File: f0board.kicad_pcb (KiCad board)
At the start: 2 copper layers, 31 x 18.3 mm, 28 parts, among them P1 CONN_12, P2 CONN_12, SW1 SW_PUSH, U1 STM32F303CCT6, U2 MCP1700, U3 MAX3051, X1 XTAL-SMD-4-PADS

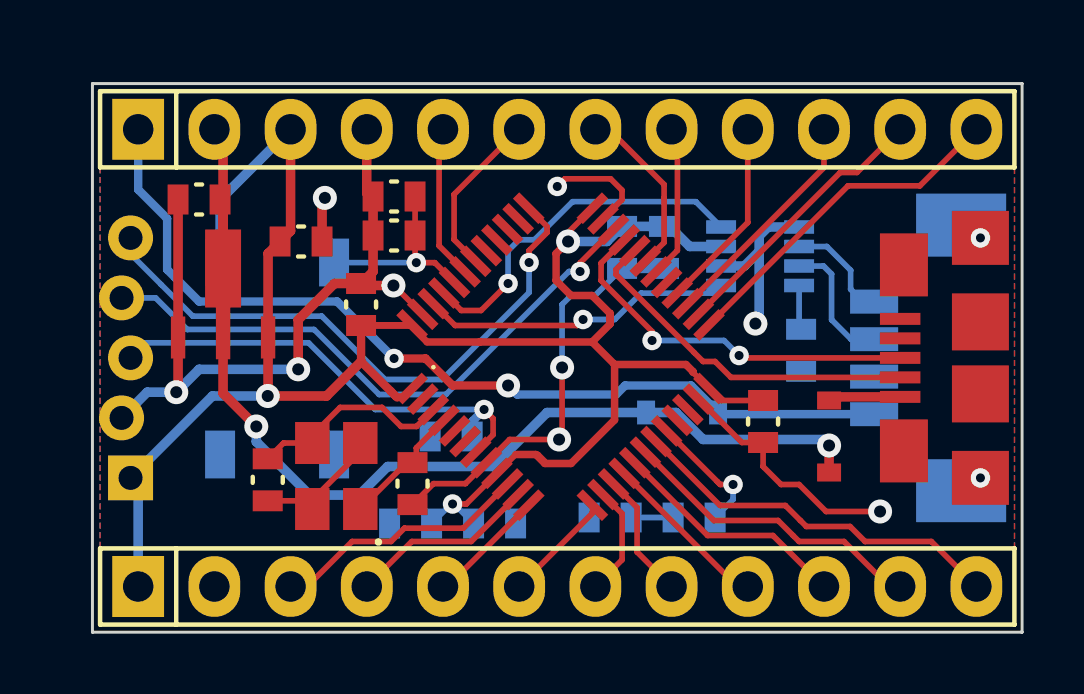
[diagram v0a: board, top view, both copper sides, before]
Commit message: inch grid alignment.
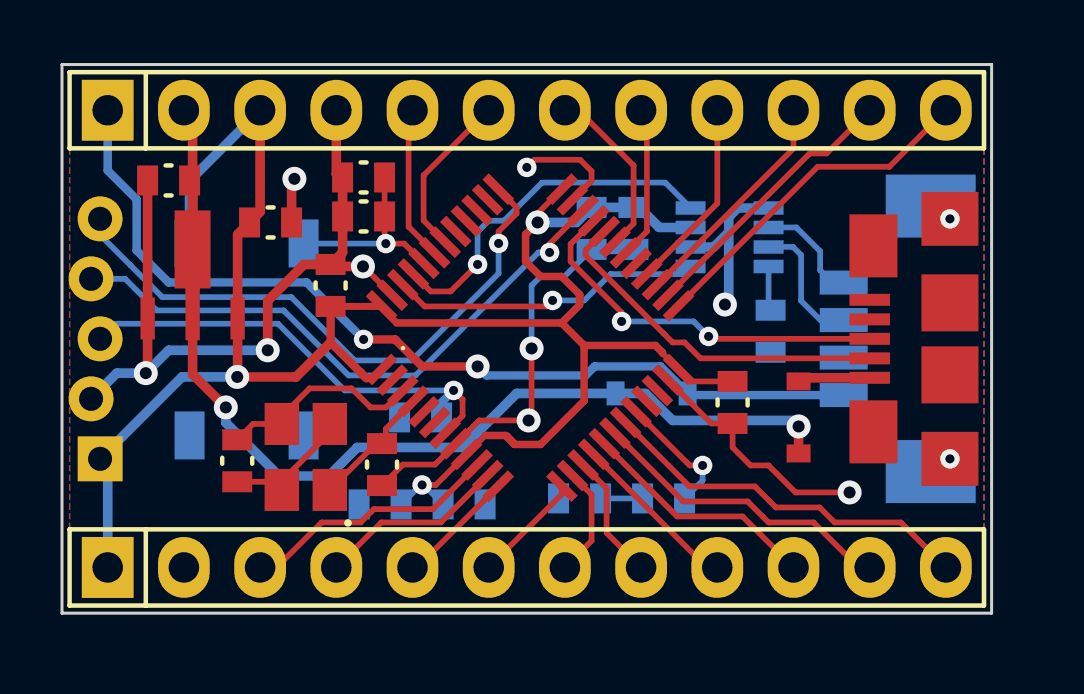
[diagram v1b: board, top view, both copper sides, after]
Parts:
- moved R3 1.20 mm to (50.0, 32.8)
- moved C7 1.20 mm to (35.4, 31.2)
- moved P1 1.20 mm to (41.9, 25.4)
- moved C12 1.20 mm to (33.4, 29.1)
- moved C4 1.20 mm to (38.4, 35.6)
- moved P2 1.20 mm to (41.9, 40.6)
- moved X1 1.20 mm to (34.5, 37.0)
- moved C11 1.20 mm to (30.0, 27.7)
- moved CONN1 1.20 mm to (27.7, 33.0)
- moved U2 1.20 mm to (30.8, 31.6)
- moved C2 1.20 mm to (45.5, 29.3)
- moved C3 1.20 mm to (44.1, 29.3)
- moved U3 1.20 mm to (47.4, 30.6)
- moved C1 1.20 mm to (36.5, 28.9)
- moved C10 1.20 mm to (32.3, 37.1)
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
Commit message: Move LED for silkscreen.
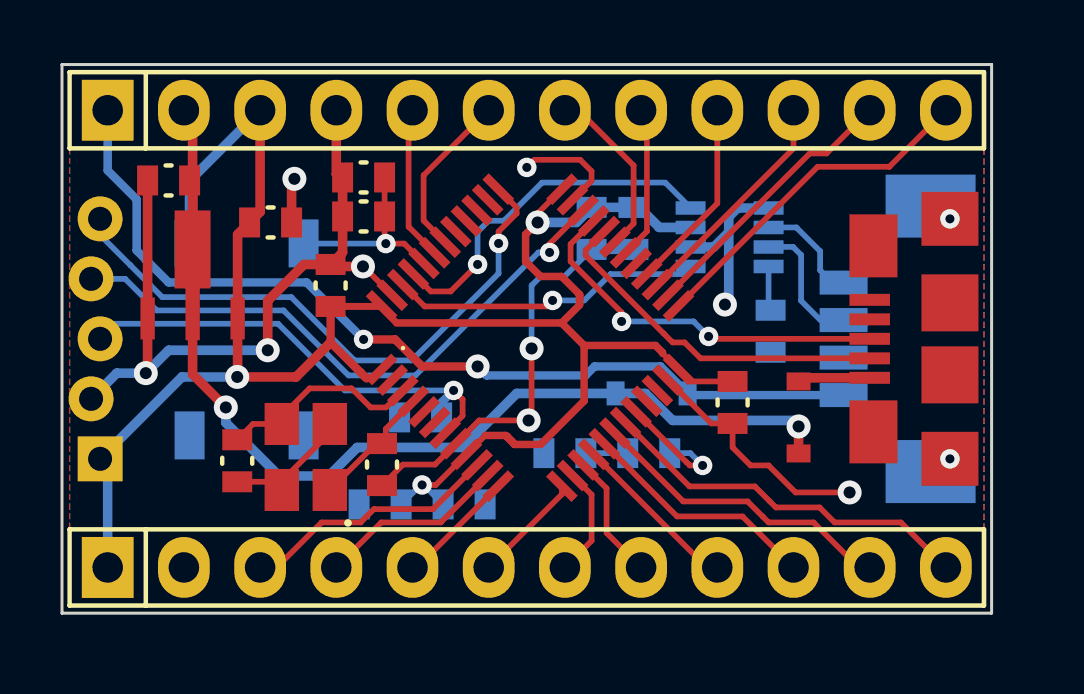
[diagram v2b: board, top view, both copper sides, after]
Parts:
- moved D1 1.59 mm to (46.0, 36.8)
- moved R1 1.59 mm to (43.2, 36.8)

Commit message: Move more compontents for silkscreen
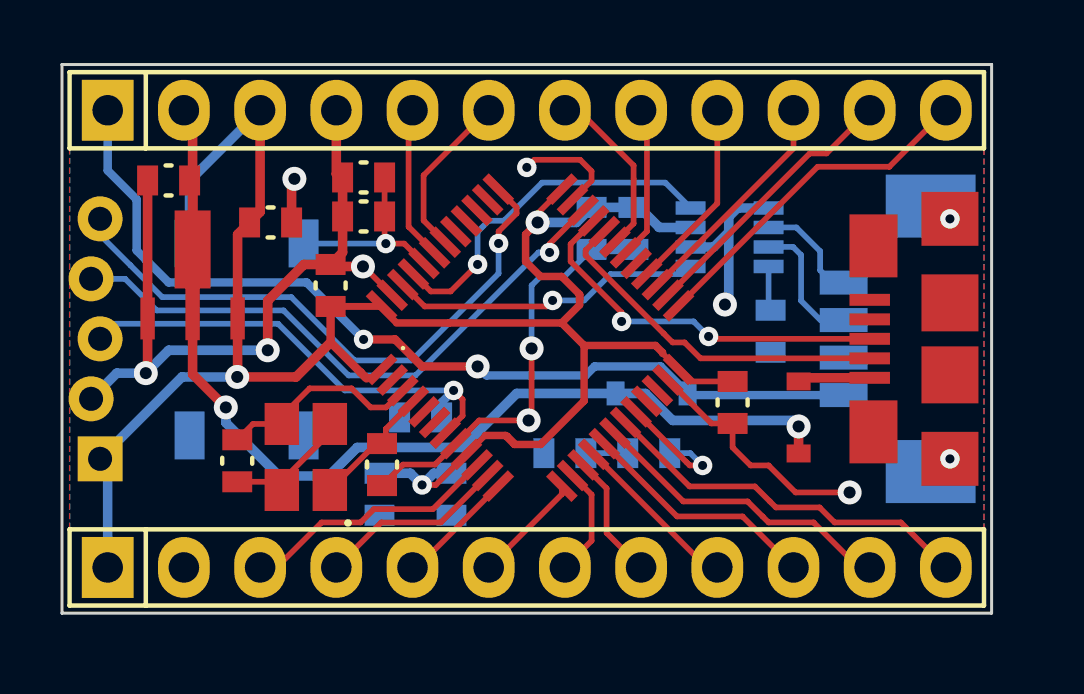
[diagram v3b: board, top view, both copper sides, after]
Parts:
- moved C6 0.54 mm to (39.4, 38.2), turned to 270 degrees
- moved C8 0.34 mm to (37.0, 38.2), turned to 270 degrees
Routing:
- net VCC: track 77.7 -> 78.6 mm
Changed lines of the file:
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@@
     (thickness 1.6)
     (drawings 6)
-    (tracks 361)
+    (tracks 363)
     (zones 0)
     (modules 28)
@@
   )
   (setup
-    (last_trace_width 0.19)
+    (last_trace_width 0.32)
     (user_trace_width 0.17)
     (user_trace_width 0.19)
@@
     (uvia_min_size 0.508)
     (uvia_min_drill 0.127)
-    (pcb_text_width 0.3)
-    (pcb_text_size 1.5 1.5)
+    (pcb_text_width 0.25)
+    (pcb_text_size 1 1)
     (mod_edge_width 0.15)
     (mod_text_size 1 1)
@@
   )
   (module _std:_0603 (layer B.Cu)
-    (at 39.82 38.54)
-    (fp_text reference C6 (at 0 0) (layer B.SilkS) hide
-      (effects (font (size 0.5 0.5) (thickness 0.125)) (justify mirror))
-    )
-    (fp_text value 1uF (at 0 0) (layer B.SilkS) hide
+    (at 39.4 38.2 270)
+    (fp_text reference C6 (at 0 0 270) (layer B.SilkS) hide
+      (effects (font (size 0.5 0.5) (thickness 0.125)) (justify mirror))
+    )
+    (fp_text value 1uF (at 0 0 270) (layer B.SilkS) hide
       (effects (font (size 0.5 0.5) (thickness 0.125)) (justify mirror))
     )
     (fp_line (start 0.1 -0.5) (end -0.1 -0.5) (layer B.SilkS) (width 0.15))
     (fp_line (start 0.1 0.5) (end -0.1 0.5) (layer B.SilkS) (width 0.15))
-    (pad 2 smd rect (at 0.7 0) (size 0.7 1) (layers B.Cu B.Mask)
-      (net 1 GND))
-    (pad 1 smd rect (at -0.7 0) (size 0.7 1) (layers B.Cu B.Mask)
+    (pad 2 smd rect (at 0.7 0 270) (size 0.7 1) (layers B.Cu B.Mask)
+      (net 1 GND))
+    (pad 1 smd rect (at -0.7 0 270) (size 0.7 1) (layers B.Cu B.Mask)
       (net 3 VCC))
   )
@@
   )
   (module _std:_0603 (layer B.Cu)
-    (at 37.02 38.54 180)
-    (fp_text reference C8 (at 0 0 180) (layer B.SilkS) hide
-      (effects (font (size 0.5 0.5) (thickness 0.125)) (justify mirror))
-    )
-    (fp_text value 10nF (at 0 0 180) (layer B.SilkS) hide
+    (at 37 38.2 270)
+    (fp_text reference C8 (at 0 0 270) (layer B.SilkS) hide
+      (effects (font (size 0.5 0.5) (thickness 0.125)) (justify mirror))
+    )
+    (fp_text value 10nF (at 0 0 270) (layer B.SilkS) hide
       (effects (font (size 0.5 0.5) (thickness 0.125)) (justify mirror))
     )
     (fp_line (start 0.1 -0.5) (end -0.1 -0.5) (layer B.SilkS) (width 0.15))
     (fp_line (start 0.1 0.5) (end -0.1 0.5) (layer B.SilkS) (width 0.15))
-    (pad 2 smd rect (at 0.7 0 180) (size 0.7 1) (layers B.Cu B.Mask)
-      (net 1 GND))
-    (pad 1 smd rect (at -0.7 0 180) (size 0.7 1) (layers B.Cu B.Mask)
+    (pad 2 smd rect (at 0.7 0 270) (size 0.7 1) (layers B.Cu B.Mask)
+      (net 1 GND))
+    (pad 1 smd rect (at -0.7 0 270) (size 0.7 1) (layers B.Cu B.Mask)
       (net 3 VCC))
   )
@@
   (segment (start 38.484214 30.504466) (end 37.824748 29.845) (width 0.19) (layer F.Cu) (net 2))
   (segment (start 37.17 29.804) (end 37.17 28.94) (width 0.19) (layer F.Cu) (net 2))
+  (segment (start 38.42 37.89) (end 38.81 37.5) (width 0.32) (layer B.Cu) (net 3))
+  (segment (start 38.81 37.5) (end 39.4 37.5) (width 0.32) (layer B.Cu) (net 3))
+  (segment (start 37 37.5) (end 38.03 37.5) (width 0.32) (layer B.Cu) (net 3))
+  (segment (start 38.876854 37.89) (end 38.42 37.89) (width 0.19) (layer F.Cu) (net 3))
+  (segment (start 38.876854 37.89) (end 39.898427 36.868427) (width 0.19) (layer F.Cu) (net 3))
+  (via (at 38.42 37.89) (size 0.65) (drill 0.3) (layers F.Cu B.Cu) (net 3))
+  (segment (start 38.03 37.5) (end 38.42 37.89) (width 0.32) (layer B.Cu) (net 3))
   (segment (start 45.466 28.637) (end 45.655 28.637) (width 0.32) (layer B.Cu) (net 3))
   (segment (start 45.655 28.637) (end 46.325 29.307) (width 0.32) (layer B.Cu) (net 3))
@@
   (segment (start 32.27 34.278) (end 32.258 34.29) (width 0.32) (layer F.Cu) (net 3))
   (segment (start 30.67 35.878) (end 30.67 36.24) (width 0.32) (layer B.Cu) (net 3))
-  (segment (start 37.72 38.54) (end 38.37 37.89) (width 0.19) (layer B.Cu) (net 3))
-  (via (at 38.42 37.89) (size 0.65) (drill 0.3) (layers F.Cu B.Cu) (net 3))
-  (segment (start 38.47 37.89) (end 39.12 38.54) (width 0.19) (layer B.Cu) (net 3))
   (segment (start 38.37 37.89) (end 38.47 37.89) (width 0.19) (layer B.Cu) (net 3))
-  (segment (start 39.898427 36.868427) (end 38.876854 37.89) (width 0.19) (layer F.Cu) (net 3))
-  (segment (start 38.876854 37.89) (end 38.42 37.89) (width 0.19) (layer F.Cu) (net 3))
   (segment (start 37.02 31.94) (end 35.37 31.94) (width 0.23) (layer F.Cu) (net 3))
   (segment (start 32.67 29.14) (end 32.47 29.14) (width 0.28) (layer F.Cu) (net 3))
@@
   (segment (start 33.744 35.598) (end 34.671 34.671) (width 0.19) (layer F.Cu) (net 6))
   (segment (start 33.744 35.857) (end 33.744 35.598) (width 0.19) (layer F.Cu) (net 6))
+  (segment (start 36.258 36.64) (end 35.306 37.592) (width 0.32) (layer B.Cu) (net 7))
+  (segment (start 35.306 37.592) (end 33.655 37.592) (width 0.32) (layer B.Cu) (net 7))
   (segment (start 39.77 36.64) (end 36.258 36.64) (width 0.32) (layer B.Cu) (net 7))
+  (segment (start 44.87 34.84) (end 41.57 34.84) (width 0.32) (layer B.Cu) (net 7))
   (segment (start 39.77 36.64) (end 41.57 34.84) (width 0.32) (layer B.Cu) (net 7))
-  (segment (start 44.87 34.84) (end 41.57 34.84) (width 0.32) (layer B.Cu) (net 7))
   (segment (start 30.77 34.199) (end 30.77 30.94) (width 0.32) (layer F.Cu) (net 7))
   (segment (start 31.877 35.306) (end 30.77 34.199) (width 0.32) (layer F.Cu) (net 7))
@@
   (segment (start 31.877 35.814) (end 31.877 35.306) (width 0.32) (layer B.Cu) (net 7))
   (segment (start 33.655 37.592) (end 31.877 35.814) (width 0.32) (layer B.Cu) (net 7))
-  (segment (start 35.306 37.592) (end 33.655 37.592) (width 0.32) (layer B.Cu) (net 7))
-  (segment (start 36.258 36.64) (end 35.306 37.592) (width 0.32) (layer B.Cu) (net 7))
   (segment (start 50.97 36.84) (end 50.97 35.94) (width 0.32) (layer F.Cu) (net 7))
   (segment (start 45.87 34.84) (end 44.87 34.84) (width 0.32) (layer B.Cu) (net 7))

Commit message: Begin  with silkscreen pin tags, some space problems.
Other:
- board text added: "+"
- board text added: "+5"
- board text added: "+C"
- board text added: "-"
- board text added: "A0"
- board text added: "A1"
- board text added: "A10"
- board text added: "A2"
- board text added: "A3"
- board text added: "A4"
- board text added: "A5"
- board text added: "A6"
- board text added: "A7"
- board text added: "A9"
- board text added: "B 14"
- board text added: "B0"
- board text added: "B1"
- board text added: "B15"
- board text added: "B6"
- board text added: "B7"
- board text added: "C"
- board text added: "D"
- board text added: "R"
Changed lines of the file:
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@@
     (area 15.622001 17.978 57.663643 42.239001)
     (thickness 1.6)
-    (drawings 6)
+    (drawings 37)
     (tracks 363)
     (zones 0)
@@
   )
   (setup
-    (last_trace_width 0.32)
+    (last_trace_width 0.36)
     (user_trace_width 0.17)
     (user_trace_width 0.19)
@@
     (zone_45_only no)
     (trace_min 0.16)
-    (segment_width 0.2)
+    (segment_width 0.25)
     (edge_width 0.1)
     (via_size 0.889)
@@
       (net 16 /USB_DP) (solder_mask_margin 0.15) (clearance 0.24))
   )
+  (gr_text + (at 29.464 37.084 90) (layer B.SilkS)
+    (effects (font (size 1 1) (thickness 0.25)) (justify mirror))
+  )
+  (gr_text - (at 29.464 35.052 90) (layer B.SilkS)
+    (effects (font (size 1 1) (thickness 0.25)) (justify mirror))
+  )
+  (gr_text R (at 29.464 33.02 90) (layer B.SilkS)
+    (effects (font (size 1 1) (thickness 0.25)) (justify mirror))
+  )
+  (gr_text D (at 29.464 30.988 90) (layer B.SilkS)
+    (effects (font (size 1 1) (thickness 0.25)) (justify mirror))
+  )
+  (gr_text C (at 29.464 28.956 90) (layer B.SilkS)
+    (effects (font (size 1 1) (thickness 0.25)) (justify mirror))
+  )
+  (gr_text + (at 33.02 27.432 90) (layer B.SilkS)
+    (effects (font (size 1 1) (thickness 0.25)) (justify mirror))
+  )
+  (gr_text +5 (at 30.48 27.432 90) (layer B.SilkS)
+    (effects (font (size 1 1) (thickness 0.25)) (justify mirror))
+  )
+  (gr_text "B\n14" (at 50.8 27.432 90) (layer B.SilkS)
+    (effects (font (size 1 1) (thickness 0.25)) (justify mirror))
+  )
+  (gr_text B15 (at 48.26 27.94 90) (layer B.SilkS)
+    (effects (font (size 1 1) (thickness 0.25)) (justify mirror))
+  )
+  (gr_text A9 (at 45.72 27.432 90) (layer B.SilkS)
+    (effects (font (size 1 1) (thickness 0.25)) (justify mirror))
+  )
+  (gr_text A10 (at 42.672 27.94 90) (layer B.SilkS)
+    (effects (font (size 1 1) (thickness 0.25)) (justify mirror))
+  )
+  (gr_text B6 (at 40.64 27.432 90) (layer B.SilkS)
+    (effects (font (size 1 1) (thickness 0.25)) (justify mirror))
+  )
+  (gr_text B7 (at 38.1 27.432 90) (layer B.SilkS)
+    (effects (font (size 1 1) (thickness 0.25)) (justify mirror))
+  )
+  (gr_text + (at 27.94 38.608 90) (layer B.SilkS)
+    (effects (font (size 1 1) (thickness 0.25)) (justify mirror))
+  )
+  (gr_text - (at 30.48 38.608 90) (layer B.SilkS)
+    (effects (font (size 1 1) (thickness 0.25)) (justify mirror))
+  )
+  (gr_line (start 52.324 37.084) (end 52.832 37.084) (angle 90) (layer B.SilkS) (width 0.25))
+  (gr_line (start 52.832 36.576) (end 52.324 37.084) (angle 90) (layer B.SilkS) (width 0.25))
+  (gr_line (start 52.832 37.084) (end 52.832 36.576) (angle 90) (layer B.SilkS) (width 0.25))
+  (gr_line (start 51.816 36.068) (end 52.832 37.084) (angle 90) (layer B.SilkS) (width 0.25))
+  (gr_text B1 (at 50.8 36.068 90) (layer B.SilkS)
+    (effects (font (size 1 1) (thickness 0.25)) (justify mirror))
+  )
+  (gr_text - (at 35.56 27.432 90) (layer B.SilkS)
+    (effects (font (size 1 1) (thickness 0.25)) (justify mirror))
+  )
+  (gr_text B0 (at 52.832 38.608 90) (layer B.SilkS)
+    (effects (font (size 1 1) (thickness 0.25)) (justify mirror))
+  )
+  (gr_text A7 (at 50.8 38.608 90) (layer B.SilkS)
+    (effects (font (size 1 1) (thickness 0.25)) (justify mirror))
+  )
+  (gr_text A6 (at 48.26 38.608 90) (layer B.SilkS)
+    (effects (font (size 1 1) (thickness 0.25)) (justify mirror))
+  )
+  (gr_text A5 (at 45.72 38.608 90) (layer B.SilkS)
+    (effects (font (size 1 1) (thickness 0.25)) (justify mirror))
+  )
+  (gr_text A4 (at 43.18 38.608 90) (layer B.SilkS)
+    (effects (font (size 1 1) (thickness 0.25)) (justify mirror))
+  )
+  (gr_text A3 (at 40.64 38.608 90) (layer B.SilkS)
+    (effects (font (size 1 1) (thickness 0.25)) (justify mirror))
+  )
+  (gr_text A2 (at 38.1 38.608 90) (layer B.SilkS)
+    (effects (font (size 1 1) (thickness 0.25)) (justify mirror))
+  )
+  (gr_text A1 (at 35.56 38.608 90) (layer B.SilkS)
+    (effects (font (size 1 1) (thickness 0.25)) (justify mirror))
+  )
+  (gr_text +C (at 27.94 27.432 90) (layer B.SilkS)
+    (effects (font (size 1 1) (thickness 0.25)) (justify mirror))
+  )
+  (gr_text A0 (at 33.02 38.608 90) (layer B.SilkS)
+    (effects (font (size 1 1) (thickness 0.25)) (justify mirror))
+  )
   (dimension 30.988 (width 0.3) (layer Cmts.User)

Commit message: Move pads for silkscreen.
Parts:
- moved U3 1.09 mm to (47.4, 31.7)
- moved C2 0.87 mm to (45.6, 30.2)
- moved C3 0.86 mm to (44.1, 30.2)
- moved R3 0.48 mm to (49.7, 33.1), turned to 180 degrees
- moved C6 0.30 mm to (39.7, 38.2)
- moved D1 0.13 mm to (46.0, 36.7)
- moved R1 0.13 mm to (43.2, 36.7)
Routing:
- net GND: track 63.6 -> 70.8 mm
- net Net-(CONN2-Pad3): track 4.95 -> 3.93 mm
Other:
- board text added: "+ C"
- board text added: "1 2"
- board text added: "B 1"
- board text added: "B13"
- board text added: "B14"
- board text removed: "+C"
- board text removed: "B 14"
- board text removed: "B1"
